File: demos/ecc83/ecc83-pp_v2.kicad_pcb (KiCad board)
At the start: 2 copper layers, 48.3 x 41.9 mm, 15 parts, among them P1 IN, P2 OUT, P3 POWER, P4 CONN_2, U1 ECC83

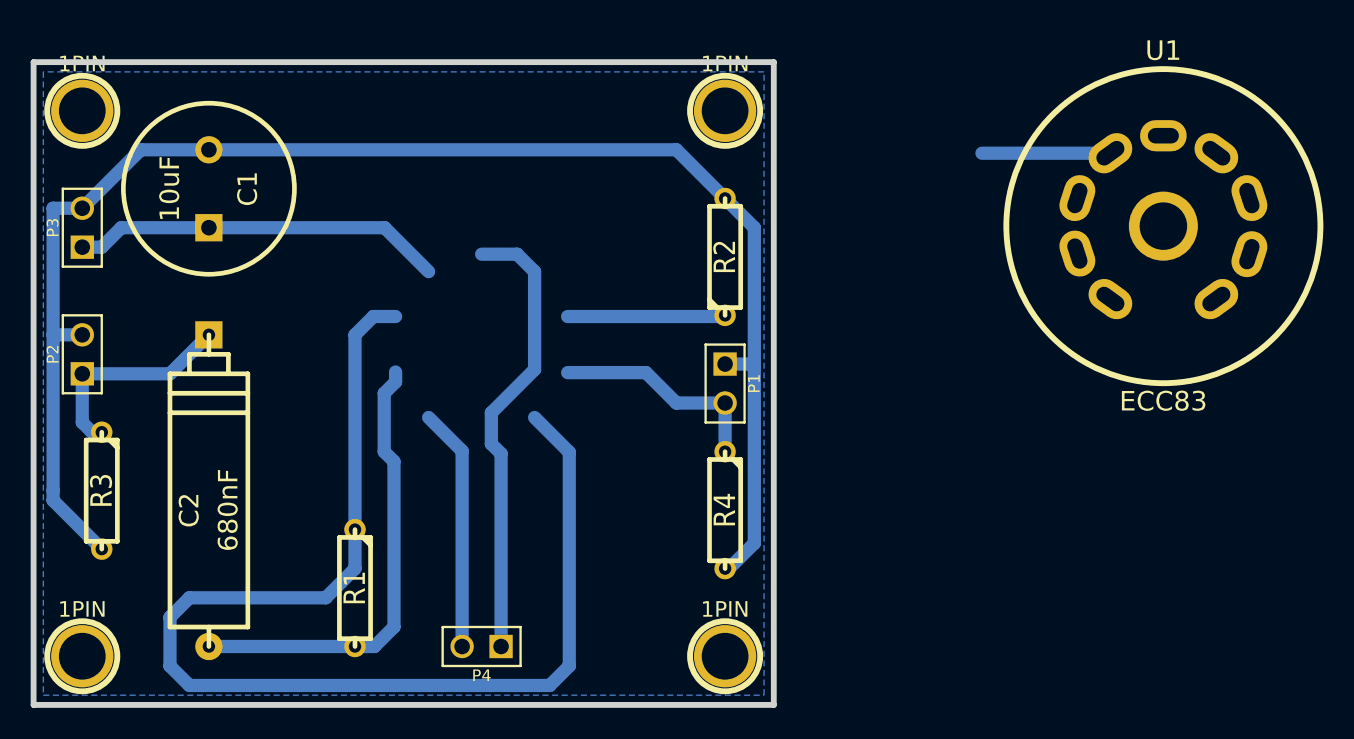
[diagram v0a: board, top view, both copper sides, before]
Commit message: Update old demo board files. Minor code cleaning.
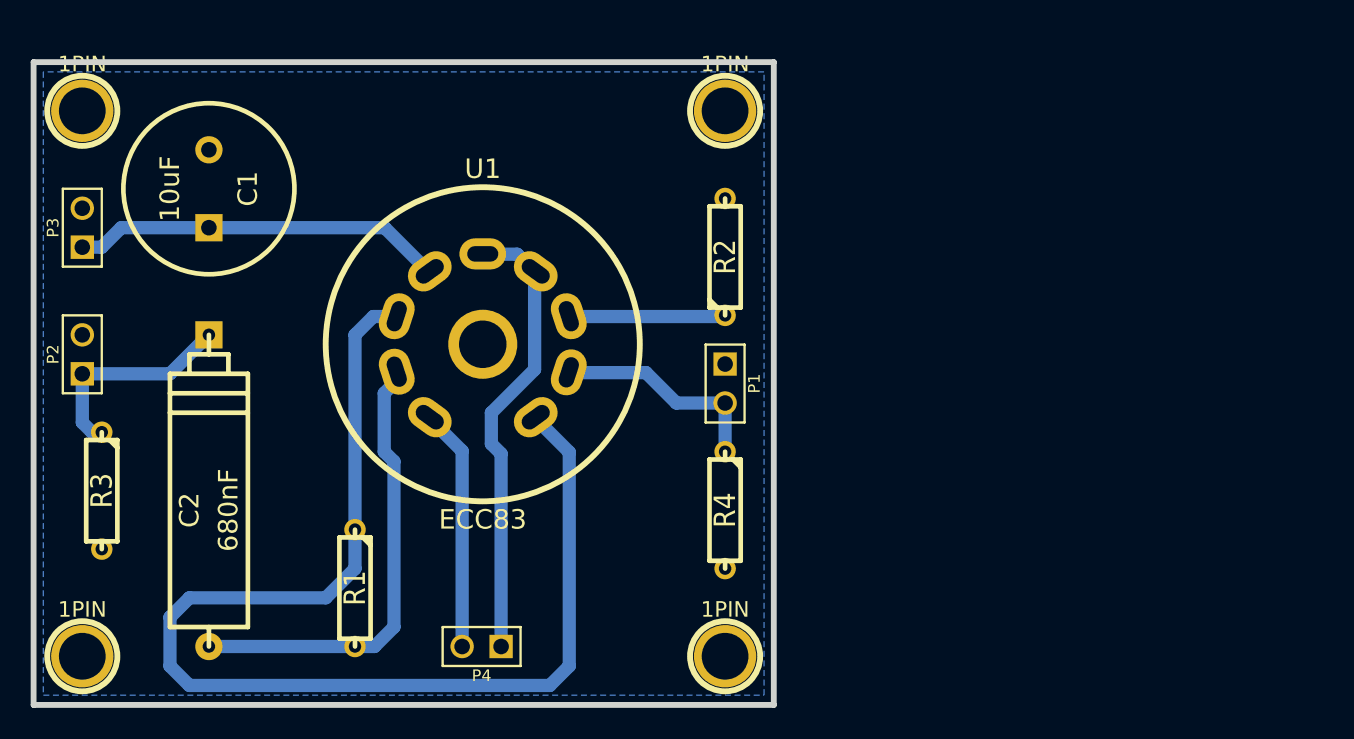
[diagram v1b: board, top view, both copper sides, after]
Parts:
- moved U1 45.0 mm to (149.3, 109.2)
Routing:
- net GND: track 99.9 -> 0.25 mm
- net Net-(C1-Pad1): track 32.7 -> 24.3 mm

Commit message: Update ecc83 demo. default KISYS3DMOD definition on Linux: add /usr/local/kicad/share/kicad/module/package3d test to find a suitable value.
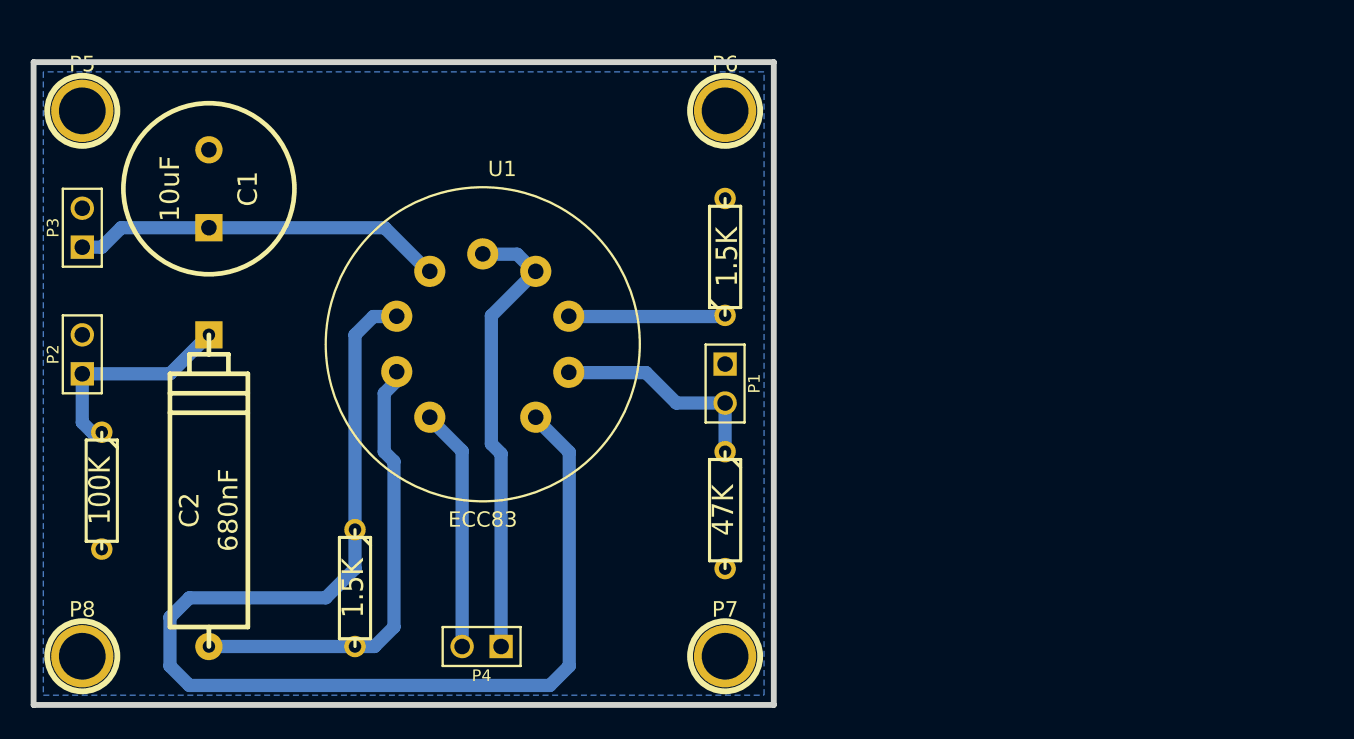
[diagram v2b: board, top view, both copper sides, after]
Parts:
- removed 1PIN (x3): P***, 1pin
- removed 1PIN: GND, 1pin
- added P5: CONN_1, connect:1pin, F.Cu at (123.2, 94.0)
- added P6: CONN_1, connect:1pin, F.Cu at (165.1, 94.0)
- added P7: CONN_1, connect:1pin, F.Cu at (165.1, 129.5)
- added P8: CONN_1, connect:1pin, F.Cu at (123.2, 129.5)
- C1: footprint C2V10 -> discret:C2V10
- C2: footprint CP8 -> discret:CP8
- P1, P2, P3, P4: footprint PIN_ARRAY_2X1 -> pin_array:pin_array_1x02
- R1, R2, R3, R4: footprint R3 -> discret:R3
- U1: footprint ECC-83-2 -> Valves:VALVE-ECC-83-1
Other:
- rule pad_to_mask_clearance: 0.254 -> 0.1

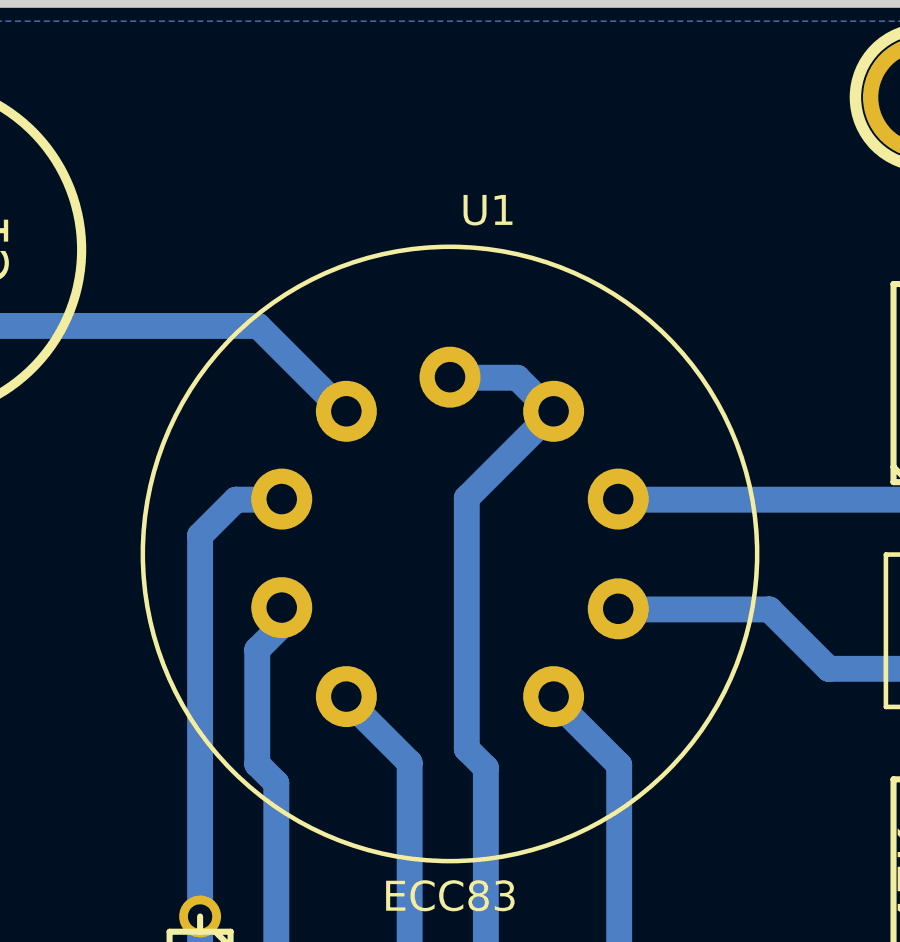
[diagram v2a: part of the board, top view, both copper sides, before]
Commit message: Fix compat with swig 3.03
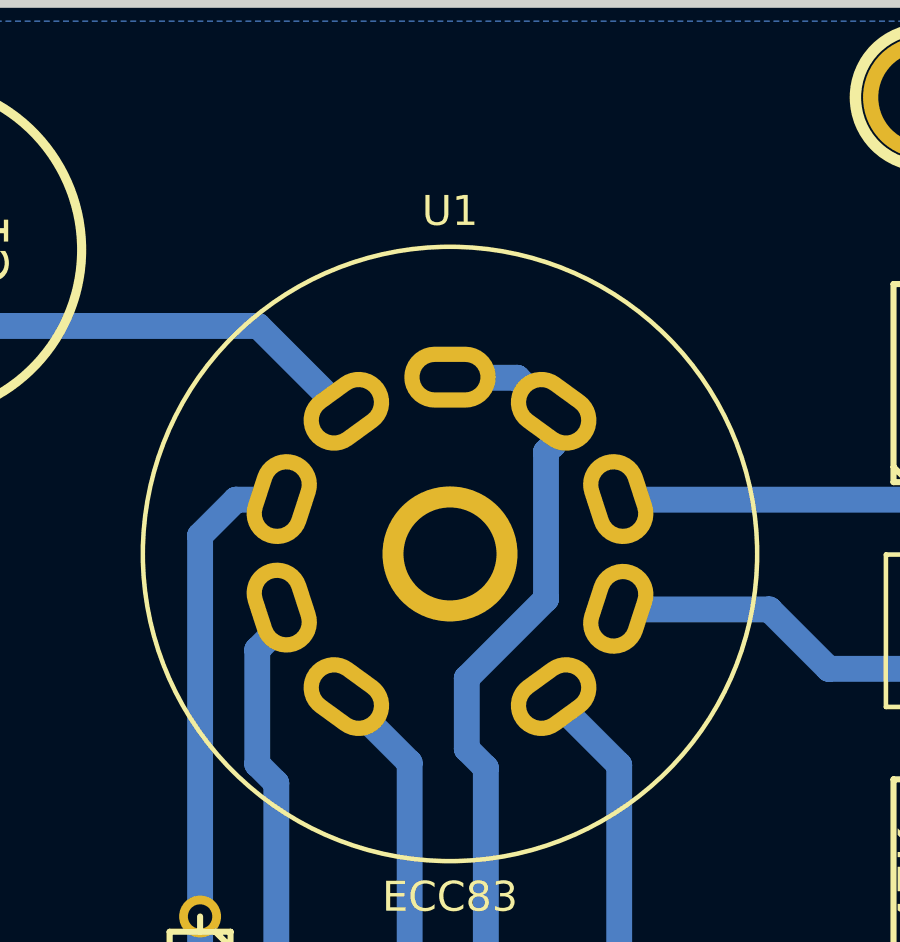
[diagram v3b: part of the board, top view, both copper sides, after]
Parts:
- U1: footprint Valves:VALVE-ECC-83-1 -> Valves:VALVE-ECC-83-2
